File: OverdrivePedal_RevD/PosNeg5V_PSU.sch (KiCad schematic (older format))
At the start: 18 parts, among them U3 TPS60400, U7 SE8233X2, U8 SE8250X2

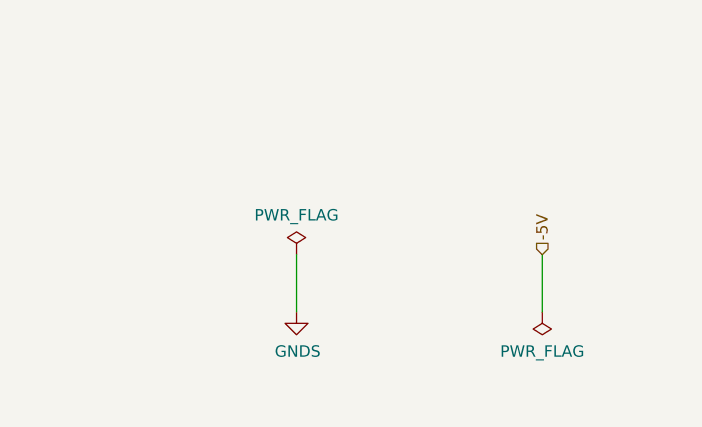
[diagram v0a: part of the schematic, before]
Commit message: Modified RevD design to use IM43 Relay instead of DG468 SW
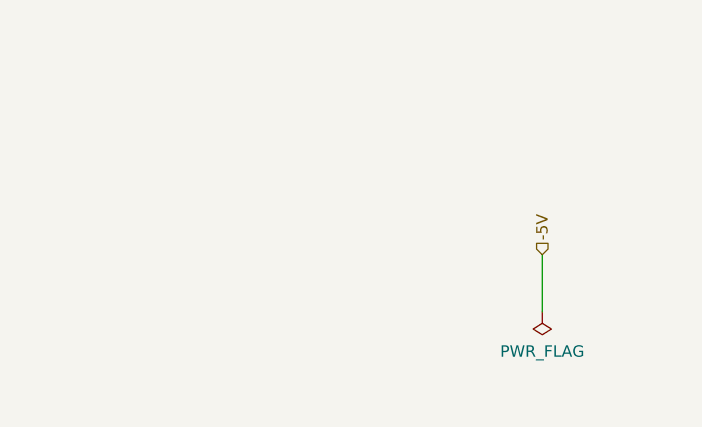
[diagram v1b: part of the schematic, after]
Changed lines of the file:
@@
 $EndComp
-Wire Wire Line
-	8925 6100 8925 6575
 Wire Wire Line
 	8925 5650 10000 5650
@@
 F 3 "~" H 6800 1675 50  0001 C CNN
 	1    6800 1675
-	1    0    0    -1
-$EndComp
-$Comp
-L power:PWR_FLAG #FLG0101
-U 1 1 5F1D2B66
-P 4600 10125
-F 0 "#FLG0101" H 4600 10200 50  0001 C CNN
-F 1 "PWR_FLAG" H 4600 10298 50  0000 C CNN
-F 2 "" H 4600 10125 50  0001 C CNN
-F 3 "~" H 4600 10125 50  0001 C CNN
-	1    4600 10125
-	1    0    0    -1
-$EndComp
-Wire Wire Line
-	4600 10125 4600 10375
-$Comp
-L power:GNDS #PWR0109
-U 1 1 5F1D3B2E
-P 4600 10375
-F 0 "#PWR0109" H 4600 10125 50  0001 C CNN
-F 1 "GNDS" H 4605 10202 50  0000 C CNN
-F 2 "" H 4600 10375 50  0001 C CNN
-F 3 "" H 4600 10375 50  0001 C CNN
-	1    4600 10375
 	1    0    0    -1
 $EndComp
@@
 Wire Wire Line
 	10550 5575 10550 5650
+Wire Wire Line
+	8925 6100 8925 6575
 $EndSCHEMATC
